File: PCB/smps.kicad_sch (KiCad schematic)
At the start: 0 parts

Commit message: ok mcu
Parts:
- added C?: 100u, symbol Device:C_Polarized
- added C?: C_Polarized, symbol Device:C_Polarized
- added D?: D_Schottky, symbol Device:D_Schottky
- added L?: L, symbol Device:L
- added R? (x3): R, symbol Device:R
- added U?: LM2576S-ADJ, Package_TO_SOT_SMD:TO-263-5_TabPin3, symbol Regulator_Switching:LM2576S-ADJ
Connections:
- net V_{Feedback}: now also R?.2
- net V_{IN}: now also C?.1, U?.1 (VIN)
- net V_{OUT}: now also C?.1, L?.2, R?.1
- new net: R?.1, R?.1, R?.2, U?.4 (FB)
- new net: D?.1 (K), L?.1, U?.2 (OUT)
- new net GND: C?.2, C?.2, D?.2 (A), R?.2, U?.3 (GND), U?.5 (~{ON}/OFF)

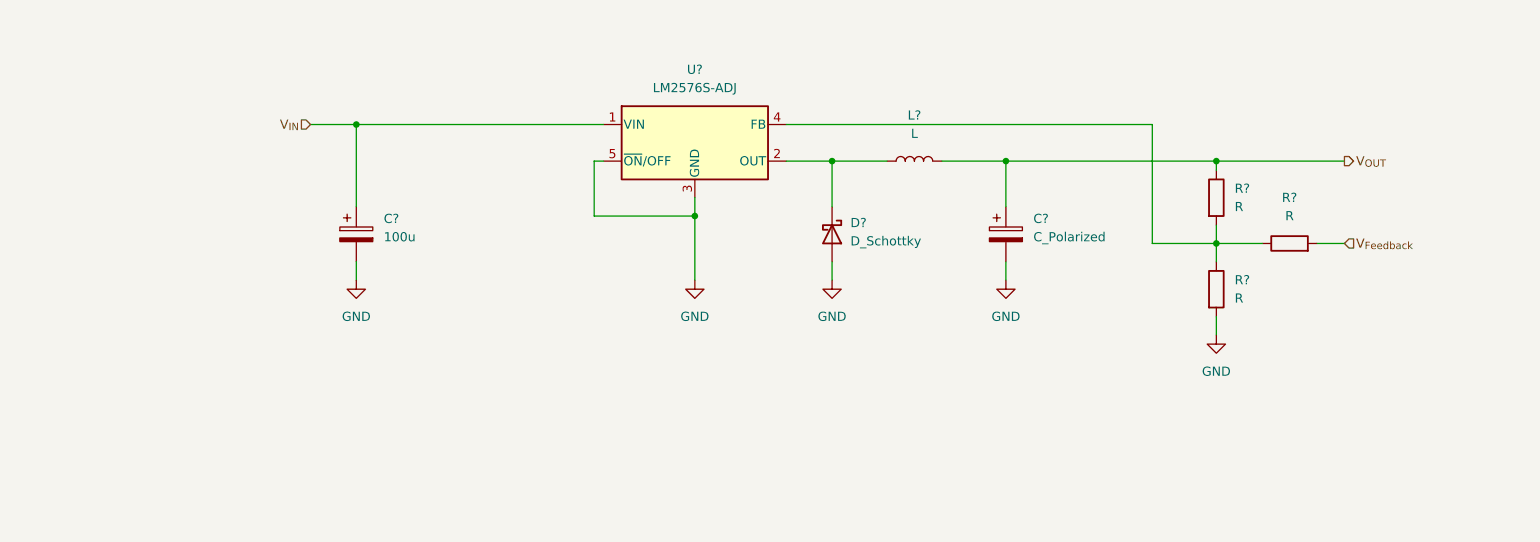
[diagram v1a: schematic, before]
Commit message: DCDC almost done
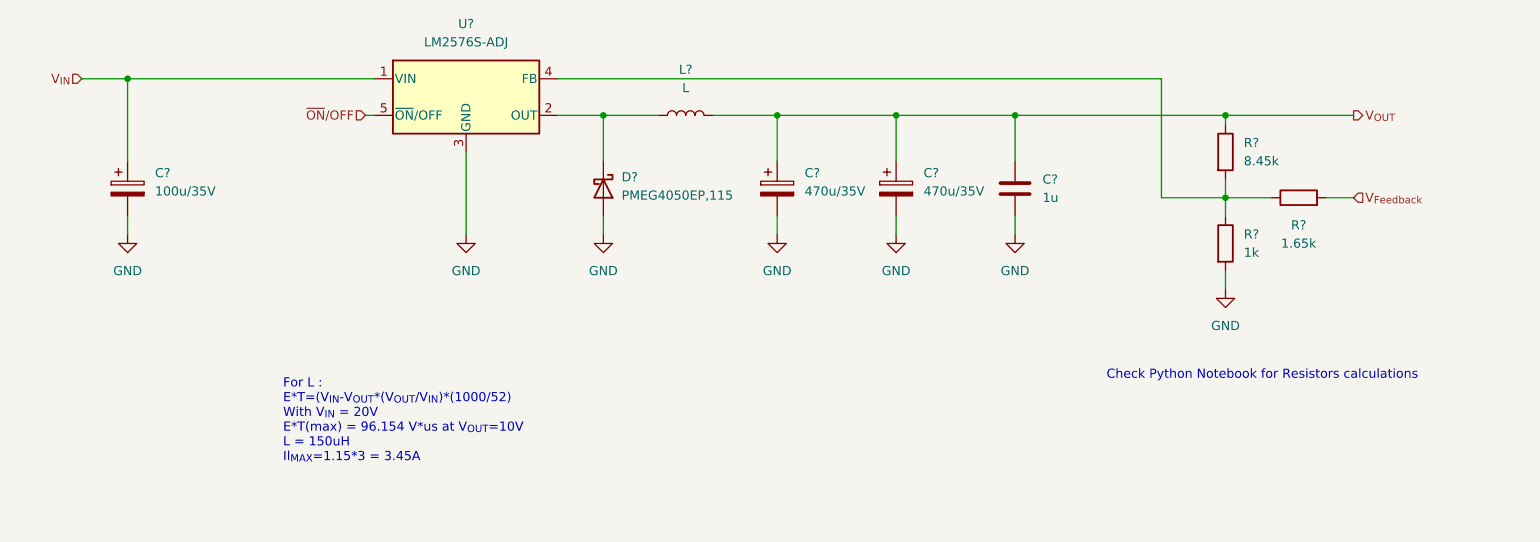
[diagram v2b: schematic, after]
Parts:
- added C?: 470u/35V, symbol Device:C_Polarized
- added C?: 1u, symbol Device:C
- C?: value 100u -> 100u/35V
- C?: value C_Polarized -> 470u/35V
- D?: value D_Schottky -> PMEG4050EP,115; footprint (none) -> Diode_SMD:D_SOD-128
- R?: value R -> 8.45k
- R?: value R -> 1.65k
- R?: value R -> 1k
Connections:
- net GND: now also C?.2, C?.2; no longer U?.5 (~{ON}/OFF)
- net V_{OUT}: now also C?.1, C?.1
- new net ~{ON}/OFF: U?.5 (~{ON}/OFF)
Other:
- note added: "Check Python Notebook for Resistors calculations"
- note added: "For L : E*T=(V_{IN}-V_{OUT}*(V_{OUT}/V_{IN})*(1000/52) With V_{IN} = 20V E*T(max) = 96.154 V*us at V_{OUT}=10V L = 150uH Il_{MAX}=1.15*3 = 3.45A"
- moved on the sheet: C?, D?, L?, R?, U?

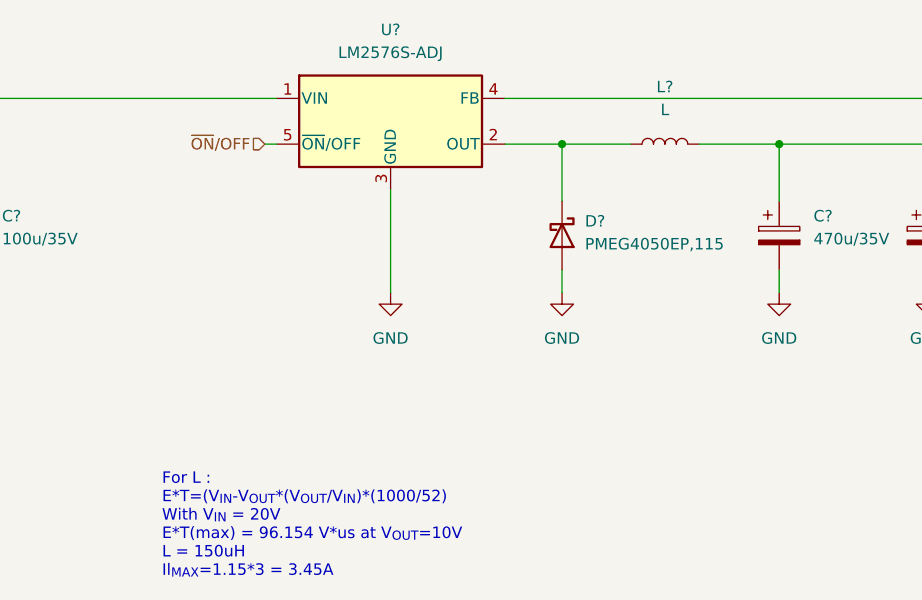
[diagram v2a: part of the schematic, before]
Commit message: upgrade usb protection + kicad 7
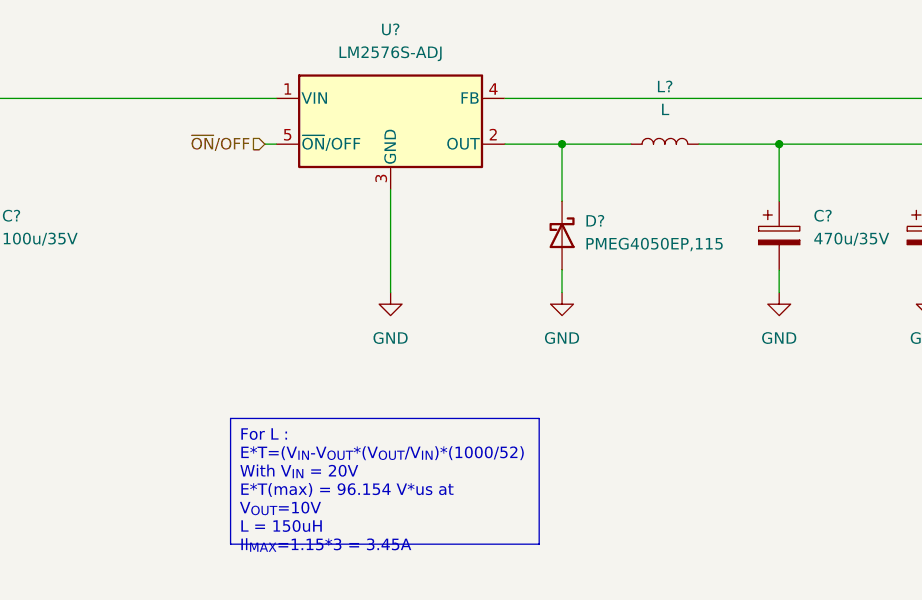
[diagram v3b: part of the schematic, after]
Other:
- note removed: "For L : E*T=(V_{IN}-V_{OUT}*(V_{OUT}/V_{IN})*(1000/52) With V_{IN} = 20V E*T(max) = 96.154 V*us at V_{OUT}=10V L = 150uH Il_{MAX}=1.15*3 = 3.45A"

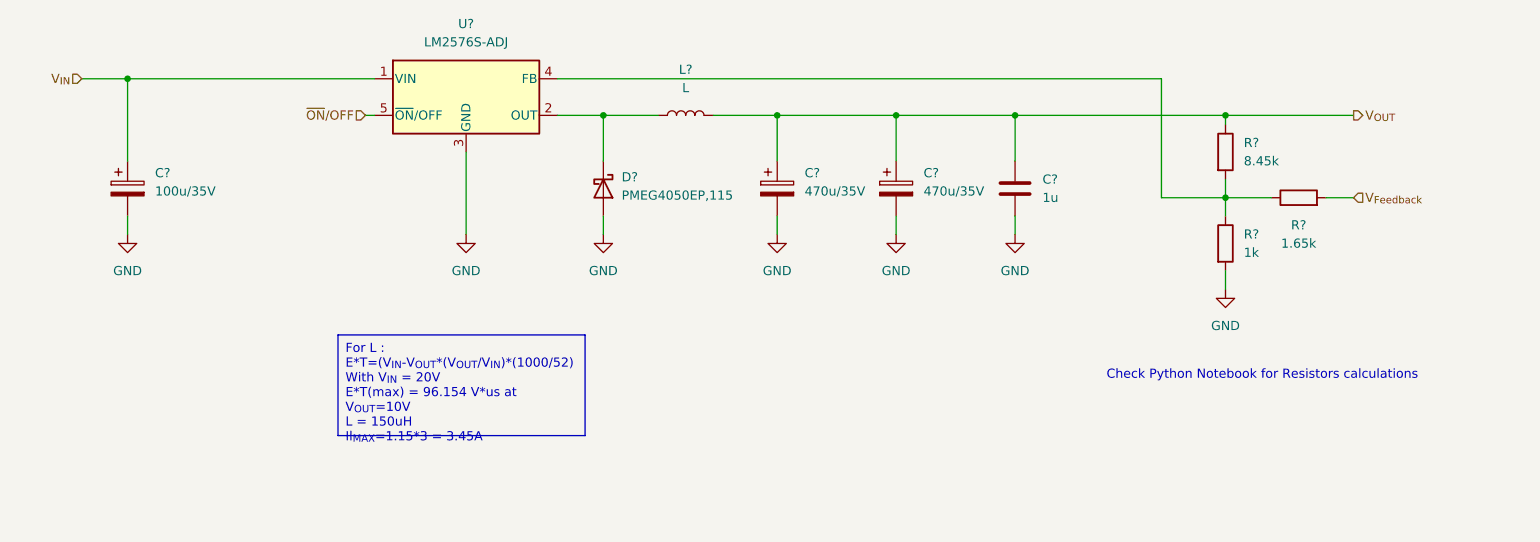
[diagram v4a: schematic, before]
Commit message: done with sch before ERC and footprints
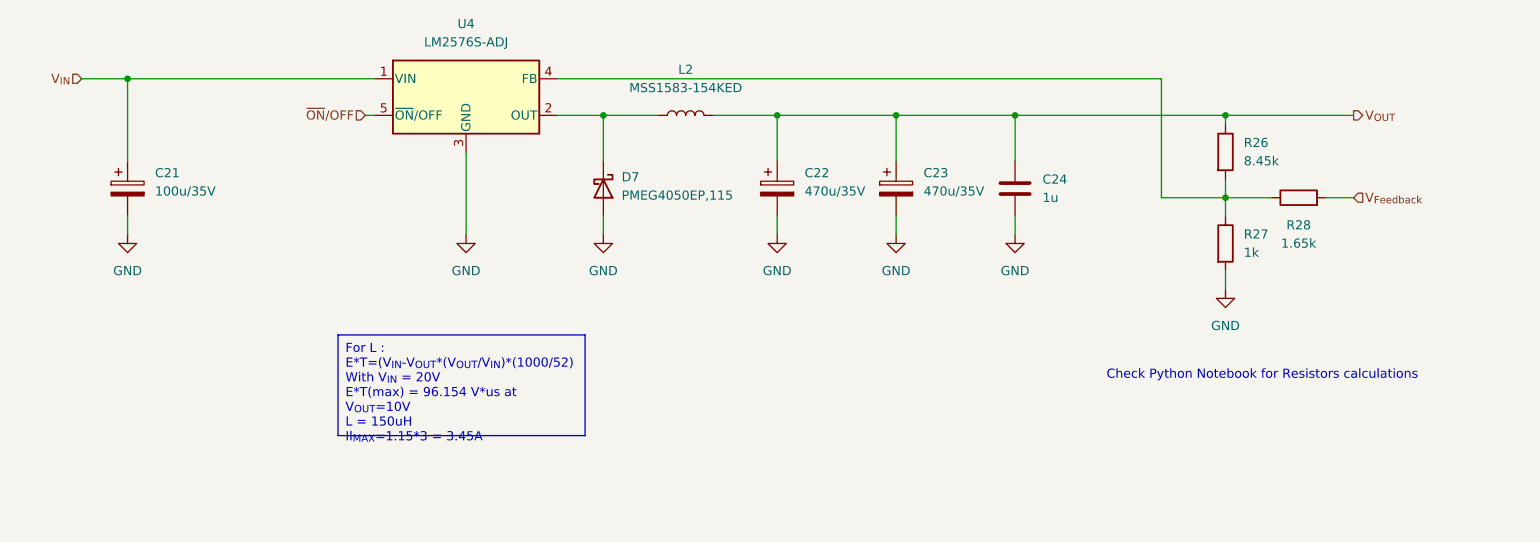
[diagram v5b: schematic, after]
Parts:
- L2: renamed from L?; value L -> MSS1583-154KED
- gave numbers to parts that had none: 9

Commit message: begin BOM
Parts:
- C21: footprint (none) -> Capacitor_SMD:CP_Elec_6.3x7.7; MPN (none) -> 865080545012; Manufacturer (none) -> Wurth Elektronik
- C22, C23: footprint (none) -> TattooSupplyFootprints:CPL_12.5_14; MPN (none) -> 865060562009; Manufacturer (none) -> Wurth Elektronik
- C24: footprint (none) -> Capacitor_SMD:C_0603_1608Metric; MPN (none) -> CGA3E1X7R1V105K080AC; Manufacturer (none) -> TDK
- D7: MPN (none) -> PMEG4050EP,115; Manufacturer (none) -> Nexperia
- L2: MPN (none) -> MSS1583-154KED; Manufacturer (none) -> Coilcraft
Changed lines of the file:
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@@
+      (effects (font (size 1.27 1.27)) hide)
+    )
+    (property "MPN" "" (at 220.98 93.98 0)
+      (effects (font (size 1.27 1.27)) hide)
+    )
+    (property "Manufacturer" "" (at 220.98 93.98 0)
       (effects (font (size 1.27 1.27)) hide)
     )
@@
       (effects (font (size 1.27 1.27)) hide)
     )
+    (property "MPN" "" (at 231.14 100.33 0)
+      (effects (font (size 1.27 1.27)) hide)
+    )
+    (property "Manufacturer" "" (at 231.14 100.33 0)
+      (effects (font (size 1.27 1.27)) hide)
+    )
     (pin "1")
     (pin "2")
@@
     )
     (property "Datasheet" "http://www.ti.com/lit/ds/symlink/lm2576.pdf" (at 115.57 86.36 0)
+      (effects (font (size 1.27 1.27)) hide)
+    )
+    (property "MPN" "" (at 115.57 86.36 0)
+      (effects (font (size 1.27 1.27)) hide)
+    )
+    (property "Manufacturer" "" (at 115.57 86.36 0)
       (effects (font (size 1.27 1.27)) hide)
     )
@@
       (effects (font (size 1.27 1.27)) hide)
     )
+    (property "MPN" "PMEG4050EP,115" (at 134.62 99.06 0)
+      (effects (font (size 1.27 1.27)) hide)
+    )
+    (property "Manufacturer" "Nexperia" (at 134.62 99.06 0)
+      (effects (font (size 1.27 1.27)) hide)
+    )
     (pin "1")
     (pin "2")
@@
       (effects (font (size 1.27 1.27)) (justify left))
     )
-    (property "Footprint" "" (at 176.2252 102.87 0)
+    (property "Footprint" "TattooSupplyFootprints:CPL_12.5_14" (at 176.2252 102.87 0)
       (effects (font (size 1.27 1.27)) hide)
     )
@@
       (effects (font (size 1.27 1.27)) hide)
     )
+    (property "MPN" "865060562009" (at 175.26 99.06 0)
+      (effects (font (size 1.27 1.27)) hide)
+    )
+    (property "Manufacturer" "Wurth Elektronik" (at 175.26 99.06 0)
+      (effects (font (size 1.27 1.27)) hide)
+    )
     (pin "1")
     (pin "2")
@@
       (effects (font (size 1.27 1.27)) (justify left))
     )
-    (property "Footprint" "" (at 69.5452 102.87 0)
+    (property "Footprint" "Capacitor_SMD:CP_Elec_6.3x7.7" (at 69.5452 102.87 0)
       (effects (font (size 1.27 1.27)) hide)
     )
@@
       (effects (font (size 1.27 1.27)) hide)
     )
+    (property "MPN" "865080545012" (at 68.58 99.06 0)
+      (effects (font (size 1.27 1.27)) hide)
+    )
+    (property "Manufacturer" "Wurth Elektronik" (at 68.58 99.06 0)
+      (effects (font (size 1.27 1.27)) hide)
+    )
     (pin "1")
     (pin "2")
@@
       (effects (font (size 1.27 1.27)) hide)
     )
+    (property "MPN" "" (at 220.98 106.68 0)
+      (effects (font (size 1.27 1.27)) hide)
+    )
+    (property "Manufacturer" "" (at 220.98 106.68 0)
+      (effects (font (size 1.27 1.27)) hide)
+    )
     (pin "1")
     (pin "2")
@@
       (effects (font (size 1.27 1.27)) hide)
     )
+    (property "MPN" "MSS1583-154KED " (at 146.05 88.9 0)
+      (effects (font (size 1.27 1.27)) hide)
+    )
+    (property "Manufacturer" "Coilcraft" (at 146.05 88.9 0)
+      (effects (font (size 1.27 1.27)) hide)
+    )
     (pin "1")
     (pin "2")
@@
       (effects (font (size 1.27 1.27)) (justify left))
     )
-    (property "Footprint" "" (at 159.7152 102.87 0)
+    (property "Footprint" "TattooSupplyFootprints:CPL_12.5_14" (at 159.7152 102.87 0)
       (effects (font (size 1.27 1.27)) hide)
     )
@@
       (effects (font (size 1.27 1.27)) hide)
     )
+    (property "MPN" "865060562009" (at 158.75 99.06 0)
+      (effects (font (size 1.27 1.27)) hide)
+    )
+    (property "Manufacturer" "Wurth Elektronik" (at 158.75 99.06 0)
+      (effects (font (size 1.27 1.27)) hide)
+    )
     (pin "1")
     (pin "2")
@@
       (effects (font (size 1.27 1.27)) (justify left))
     )
-    (property "Footprint" "" (at 192.7352 102.87 0)
+    (property "Footprint" "Capacitor_SMD:C_0603_1608Metric" (at 192.7352 102.87 0)
       (effects (font (size 1.27 1.27)) hide)
     )
@@
       (effects (font (size 1.27 1.27)) hide)
     )
+    (property "MPN" "CGA3E1X7R1V105K080AC" (at 191.77 99.06 0)
+      (effects (font (size 1.27 1.27)) hide)
+    )
+    (property "Manufacturer" "TDK" (at 191.77 99.06 0)
+      (effects (font (size 1.27 1.27)) hide)
+    )

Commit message: Resistors ok in BOM
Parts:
- R26: footprint (none) -> Resistor_SMD:R_0603_1608Metric; MPN (none) -> ERJ-3EKF8451V; Manufacturer (none) -> Panasonic
- R27: footprint (none) -> Resistor_SMD:R_0603_1608Metric; MPN (none) -> ERJ-3EKF1001V; Manufacturer (none) -> Panasonic
- R28: footprint (none) -> Resistor_SMD:R_0603_1608Metric; MPN (none) -> ERJ-3EKF1651V; Manufacturer (none) -> Panasonic
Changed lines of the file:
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@@
       (effects (font (size 1.27 1.27)) (justify left))
     )
-    (property "Footprint" "" (at 219.202 93.98 90)
+    (property "Footprint" "Resistor_SMD:R_0603_1608Metric" (at 219.202 93.98 90)
       (effects (font (size 1.27 1.27)) hide)
     )
@@
       (effects (font (size 1.27 1.27)) hide)
     )
-    (property "MPN" "" (at 220.98 93.98 0)
-      (effects (font (size 1.27 1.27)) hide)
-    )
-    (property "Manufacturer" "" (at 220.98 93.98 0)
+    (property "MPN" "ERJ-3EKF8451V" (at 220.98 93.98 0)
+      (effects (font (size 1.27 1.27)) hide)
+    )
+    (property "Manufacturer" "Panasonic" (at 220.98 93.98 0)
       (effects (font (size 1.27 1.27)) hide)
     )
@@
       (effects (font (size 1.27 1.27)))
     )
-    (property "Footprint" "" (at 231.14 102.108 90)
+    (property "Footprint" "Resistor_SMD:R_0603_1608Metric" (at 231.14 102.108 90)
       (effects (font (size 1.27 1.27)) hide)
     )
@@
       (effects (font (size 1.27 1.27)) hide)
     )
-    (property "MPN" "" (at 231.14 100.33 0)
-      (effects (font (size 1.27 1.27)) hide)
-    )
-    (property "Manufacturer" "" (at 231.14 100.33 0)
+    (property "MPN" "ERJ-3EKF1651V" (at 231.14 100.33 0)
+      (effects (font (size 1.27 1.27)) hide)
+    )
+    (property "Manufacturer" "Panasonic" (at 231.14 100.33 0)
       (effects (font (size 1.27 1.27)) hide)
     )
@@
       (effects (font (size 1.27 1.27)) (justify left))
     )
-    (property "Footprint" "" (at 219.202 106.68 90)
+    (property "Footprint" "Resistor_SMD:R_0603_1608Metric" (at 219.202 106.68 90)
       (effects (font (size 1.27 1.27)) hide)
     )
@@
       (effects (font (size 1.27 1.27)) hide)
     )
-    (property "MPN" "" (at 220.98 106.68 0)
-      (effects (font (size 1.27 1.27)) hide)
-    )
-    (property "Manufacturer" "" (at 220.98 106.68 0)
-      (effects (font (size 1.27 1.27)) hide)
-    )
+    (property "MPN" "ERJ-3EKF1001V" (at 220.98 106.68 0)
+      (effects (font (size 1.27 1.27)) hide)
+    )
+    (property "Manufacturer" "Panasonic" (at 220.98 106.68 0)
+      (effects (font (size 1.27 1.27)) hide)
+    )

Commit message: bom almost finished
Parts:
- U4: MPN (none) -> LM2576D2T-ADJR4G; Manufacturer (none) -> Onsemi
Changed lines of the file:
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@@
       (effects (font (size 1.27 1.27)) hide)
     )
-    (property "MPN" "" (at 115.57 86.36 0)
+    (property "MPN" "LM2576D2T-ADJR4G" (at 115.57 86.36 0)
       (effects (font (size 1.27 1.27)) hide)
     )
-    (property "Manufacturer" "" (at 115.57 86.36 0)
+    (property "Manufacturer" "Onsemi" (at 115.57 86.36 0)
       (effects (font (size 1.27 1.27)) hide)
     )
